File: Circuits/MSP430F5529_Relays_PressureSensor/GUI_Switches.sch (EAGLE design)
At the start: 7 parts

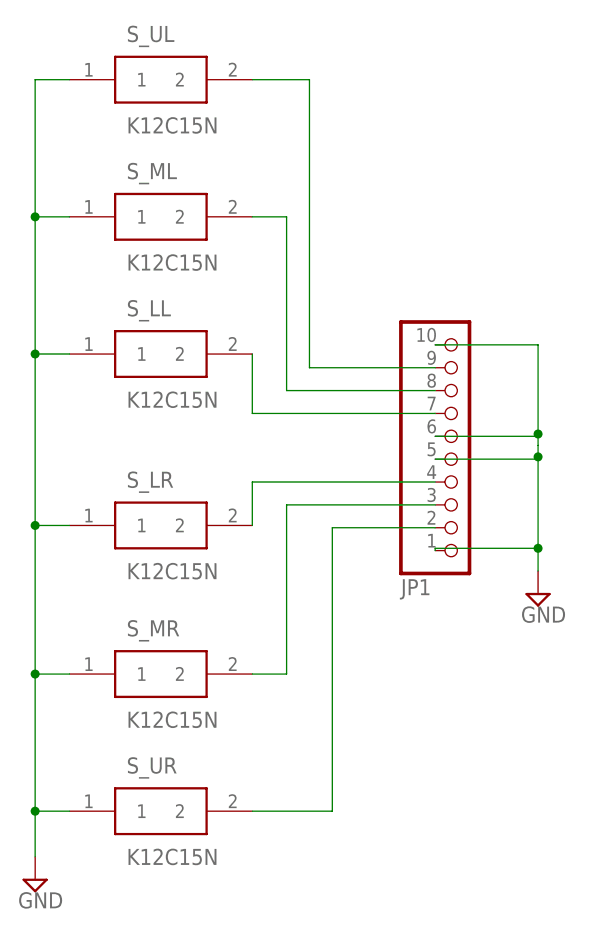
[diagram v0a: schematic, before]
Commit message: Add power supply and connector for GUI_Switches board
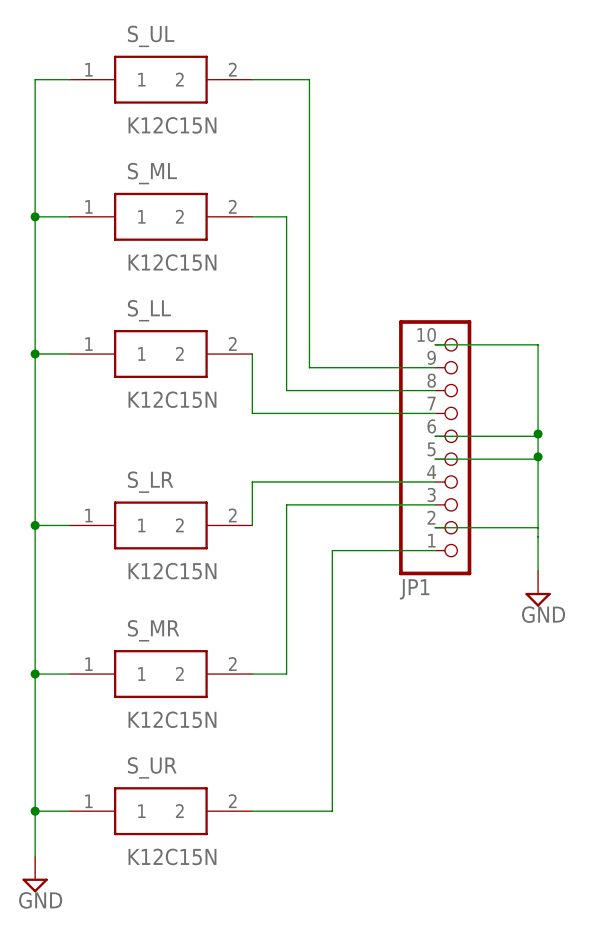
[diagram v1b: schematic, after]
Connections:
- net GND: now also JP1.2; no longer JP1.1
- net N$6: now also JP1.1; no longer JP1.2
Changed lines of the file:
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@@
 <setting verticaltext="up"/>
 </settings>
-<grid distance="0.05" unitdist="inch" unit="inch" style="lines" multiple="1" display="no" altdistance="0.01" altunitdist="inch" altunit="inch"/>
+<grid distance="0.1" unitdist="inch" unit="inch" style="lines" multiple="1" display="no" altdistance="0.01" altunitdist="inch" altunit="inch"/>
 <layers>
-<layer number="1" name="Top" color="4" fill="1" visible="yes" active="no"/>
-<layer number="2" name="Route2" color="16" fill="1" visible="yes" active="no"/>
-<layer number="3" name="Route3" color="17" fill="1" visible="yes" active="no"/>
-<layer number="4" name="Route4" color="18" fill="1" visible="yes" active="no"/>
-<layer number="5" name="Route5" color="19" fill="1" visible="yes" active="no"/>
-<layer number="6" name="Route6" color="25" fill="1" visible="yes" active="no"/>
-<layer number="7" name="Route7" color="26" fill="1" visible="yes" active="no"/>
-<layer number="8" name="Route8" color="27" fill="1" visible="yes" active="no"/>
-<layer number="9" name="Route9" color="28" fill="1" visible="yes" active="no"/>
-<layer number="10" name="Route10" color="29" fill="1" visible="yes" active="no"/>
-<layer number="11" name="Route11" color="30" fill="1" visible="yes" active="no"/>
-<layer number="12" name="Route12" color="20" fill="1" visible="yes" active="no"/>
-<layer number="13" name="Route13" color="21" fill="1" visible="yes" active="no"/>
-<layer number="14" name="Route14" color="22" fill="1" visible="yes" active="no"/>
-<layer number="15" name="Route15" color="23" fill="1" visible="yes" active="no"/>
-<layer number="16" name="Bottom" color="1" fill="1" visible="yes" active="no"/>
-<layer number="17" name="Pads" color="2" fill="1" visible="yes" active="no"/>
-<layer number="18" name="Vias" color="2" fill="1" visible="yes" active="no"/>
-<layer number="19" name="Unrouted" color="6" fill="1" visible="yes" active="no"/>
-<layer number="20" name="Dimension" color="24" fill="1" visible="yes" active="no"/>
-<layer number="21" name="tPlace" color="7" fill="1" visible="yes" active="no"/>
-<layer number="22" name="bPlace" color="7" fill="1" visible="yes" active="no"/>
-<layer number="23" name="tOrigins" color="15" fill="1" visible="yes" active="no"/>
-<layer number="24" name="bOrigins" color="15" fill="1" visible="yes" active="no"/>
-<layer number="25" name="tNames" color="7" fill="1" visible="yes" active="no"/>
-<layer number="26" name="bNames" color="7" fill="1" visible="yes" active="no"/>
-<layer number="27" name="tValues" color="7" fill="1" visible="yes" active="no"/>
-<layer number="28" name="bValues" color="7" fill="1" visible="yes" active="no"/>
+<layer number="1" name="Top" color="4" fill="1" visible="no" active="no"/>
+<layer number="2" name="Route2" color="16" fill="1" visible="no" active="no"/>
+<layer number="3" name="Route3" color="17" fill="1" visible="no" active="no"/>
+<layer number="4" name="Route4" color="18" fill="1" visible="no" active="no"/>
+<layer number="5" name="Route5" color="19" fill="1" visible="no" active="no"/>
+<layer number="6" name="Route6" color="25" fill="1" visible="no" active="no"/>
+<layer number="7" name="Route7" color="26" fill="1" visible="no" active="no"/>
+<layer number="8" name="Route8" color="27" fill="1" visible="no" active="no"/>
+<layer number="9" name="Route9" color="28" fill="1" visible="no" active="no"/>
+<layer number="10" name="Route10" color="29" fill="1" visible="no" active="no"/>
+<layer number="11" name="Route11" color="30" fill="1" visible="no" active="no"/>
+<layer number="12" name="Route12" color="20" fill="1" visible="no" active="no"/>
+<layer number="13" name="Route13" color="21" fill="1" visible="no" active="no"/>
+<layer number="14" name="Route14" color="22" fill="1" visible="no" active="no"/>
+<layer number="15" name="Route15" color="23" fill="1" visible="no" active="no"/>
+<layer number="16" name="Bottom" color="1" fill="1" visible="no" active="no"/>
+<layer number="17" name="Pads" color="2" fill="1" visible="no" active="no"/>
+<layer number="18" name="Vias" color="2" fill="1" visible="no" active="no"/>
+<layer number="19" name="Unrouted" color="6" fill="1" visible="no" active="no"/>
+<layer number="20" name="Dimension" color="24" fill="1" visible="no" active="no"/>
+<layer number="21" name="tPlace" color="7" fill="1" visible="no" active="no"/>
+<layer number="22" name="bPlace" color="7" fill="1" visible="no" active="no"/>
+<layer number="23" name="tOrigins" color="15" fill="1" visible="no" active="no"/>
+<layer number="24" name="bOrigins" color="15" fill="1" visible="no" active="no"/>
+<layer number="25" name="tNames" color="7" fill="1" visible="no" active="no"/>
+<layer number="26" name="bNames" color="7" fill="1" visible="no" active="no"/>
+<layer number="27" name="tValues" color="7" fill="1" visible="no" active="no"/>
+<layer number="28" name="bValues" color="7" fill="1" visible="no" active="no"/>
 <layer number="29" name="tStop" color="7" fill="3" visible="no" active="no"/>
 <layer number="30" name="bStop" color="7" fill="6" visible="no" active="no"/>
@@
 <layer number="35" name="tGlue" color="7" fill="4" visible="no" active="no"/>
 <layer number="36" name="bGlue" color="7" fill="5" visible="no" active="no"/>
-<layer number="37" name="tTest" color="7" fill="1" visible="yes" active="no"/>
-<layer number="38" name="bTest" color="7" fill="1" visible="yes" active="no"/>
+<layer number="37" name="tTest" color="7" fill="1" visible="no" active="no"/>
+<layer number="38" name="bTest" color="7" fill="1" visible="no" active="no"/>
 <layer number="39" name="tKeepout" color="4" fill="11" visible="no" active="no"/>
 <layer number="40" name="bKeepout" color="1" fill="11" visible="no" active="no"/>
@@
 <layer number="44" name="Drills" color="7" fill="1" visible="no" active="no"/>
 <layer number="45" name="Holes" color="7" fill="1" visible="no" active="no"/>
-<layer number="46" name="Milling" color="3" fill="1" visible="yes" active="no"/>
-<layer number="47" name="Measures" color="7" fill="1" visible="yes" active="no"/>
-<layer number="48" name="Document" color="7" fill="1" visible="yes" active="no"/>
-<layer number="49" name="Reference" color="7" fill="1" visible="yes" active="no"/>
-<layer number="51" name="tDocu" color="7" fill="1" visible="yes" active="no"/>
-<layer number="52" name="bDocu" color="7" fill="1" visible="yes" active="no"/>
+<layer number="46" name="Milling" color="3" fill="1" visible="no" active="no"/>
+<layer number="47" name="Measures" color="7" fill="1" visible="no" active="no"/>
+<layer number="48" name="Document" color="7" fill="1" visible="no" active="no"/>
+<layer number="49" name="Reference" color="7" fill="1" visible="no" active="no"/>
+<layer number="51" name="tDocu" color="7" fill="1" visible="no" active="no"/>
+<layer number="52" name="bDocu" color="7" fill="1" visible="no" active="no"/>
 <layer number="88" name="SimResults" color="9" fill="1" visible="yes" active="yes"/>
 <layer number="89" name="SimProbes" color="9" fill="1" visible="yes" active="yes"/>
@@
 <pinref part="SUPPLY3" gate="GND" pin="GND"/>
 <wire x1="59.69" y1="51.816" x2="71.12" y2="51.816" width="0.1524" layer="91"/>
-<pinref part="JP1" gate="A" pin="1"/>
-<wire x1="71.12" y1="51.816" x2="71.12" y2="41.91" width="0.1524" layer="91"/>
-<wire x1="71.12" y1="41.91" x2="71.12" y2="39.37" width="0.1524" layer="91"/>
-<wire x1="59.69" y1="41.656" x2="59.69" y2="41.91" width="0.1524" layer="91"/>
-<wire x1="59.69" y1="41.91" x2="71.12" y2="41.91" width="0.1524" layer="91"/>
-<junction x="71.12" y="41.91"/>
+<wire x1="71.12" y1="51.816" x2="71.12" y2="44.196" width="0.1524" layer="91"/>
 <pinref part="JP1" gate="A" pin="6"/>
+<wire x1="71.12" y1="43.18" x2="71.12" y2="39.37" width="0.1524" layer="91"/>
 <wire x1="59.69" y1="54.356" x2="71.12" y2="54.356" width="0.1524" layer="91"/>
-<wire x1="71.12" y1="54.356" x2="71.12" y2="53.34" width="0.1524" layer="91"/>
 <pinref part="JP1" gate="A" pin="10"/>
-<wire x1="71.12" y1="53.34" x2="71.12" y2="52.07" width="0.1524" layer="91"/>
+<wire x1="71.12" y1="54.356" x2="71.12" y2="52.07" width="0.1524" layer="91"/>
 <wire x1="71.12" y1="52.07" x2="71.12" y2="51.816" width="0.1524" layer="91"/>
 <wire x1="59.69" y1="64.516" x2="71.12" y2="64.516" width="0.1524" layer="91"/>
@@
 <wire x1="71.12" y1="54.61" x2="71.12" y2="54.356" width="0.1524" layer="91"/>
 <junction x="71.12" y="52.07"/>
+<pinref part="JP1" gate="A" pin="2"/>
+<wire x1="59.69" y1="44.196" x2="71.12" y2="44.196" width="0.1524" layer="91"/>
+<wire x1="71.12" y1="44.196" x2="71.12" y2="43.18" width="0.1524" layer="91"/>
 </segment>
 </net>
@@
 <pinref part="S_UR" gate="G$1" pin="2"/>
 <wire x1="39.37" y1="12.7" x2="48.26" y2="12.7" width="0.1524" layer="91"/>
-<wire x1="48.26" y1="12.7" x2="48.26" y2="44.196" width="0.1524" layer="91"/>
-<pinref part="JP1" gate="A" pin="2"/>
-<wire x1="59.69" y1="44.196" x2="48.26" y2="44.196" width="0.1524" layer="91"/>
-</segment>
-</net>
+<wire x1="48.26" y1="12.7" x2="48.26" y2="41.656" width="0.1524" layer="91"/>
+<pinref part="JP1" gate="A" pin="1"/>
+<wire x1="59.69" y1="41.656" x2="48.26" y2="41.656" width="0.1524" layer="91"/>
+</segment>
+</net>
